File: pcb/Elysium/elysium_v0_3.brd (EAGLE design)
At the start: 64.8 x 105.1 mm, 20 parts, among them U1 TLC5940-NT, U2 TLC5940-NT, U3 TLC5940-NT, U4 TLC5940-NT

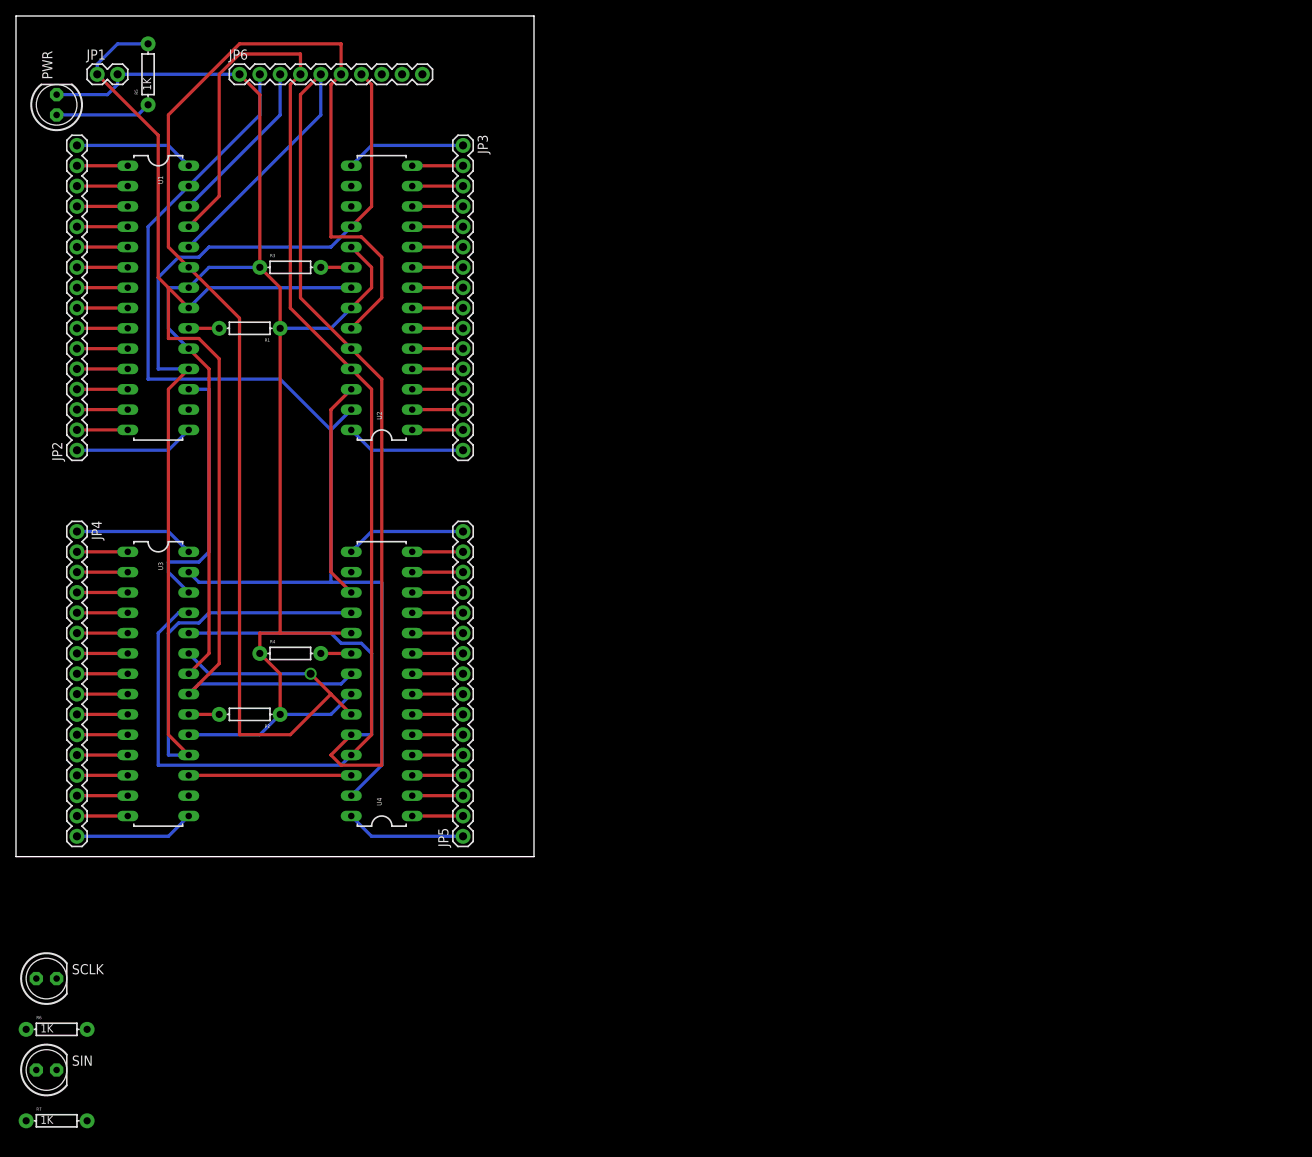
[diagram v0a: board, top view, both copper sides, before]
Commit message: Added rev_0_4 board
Rev 0_4 has status LEDs with ground planes.
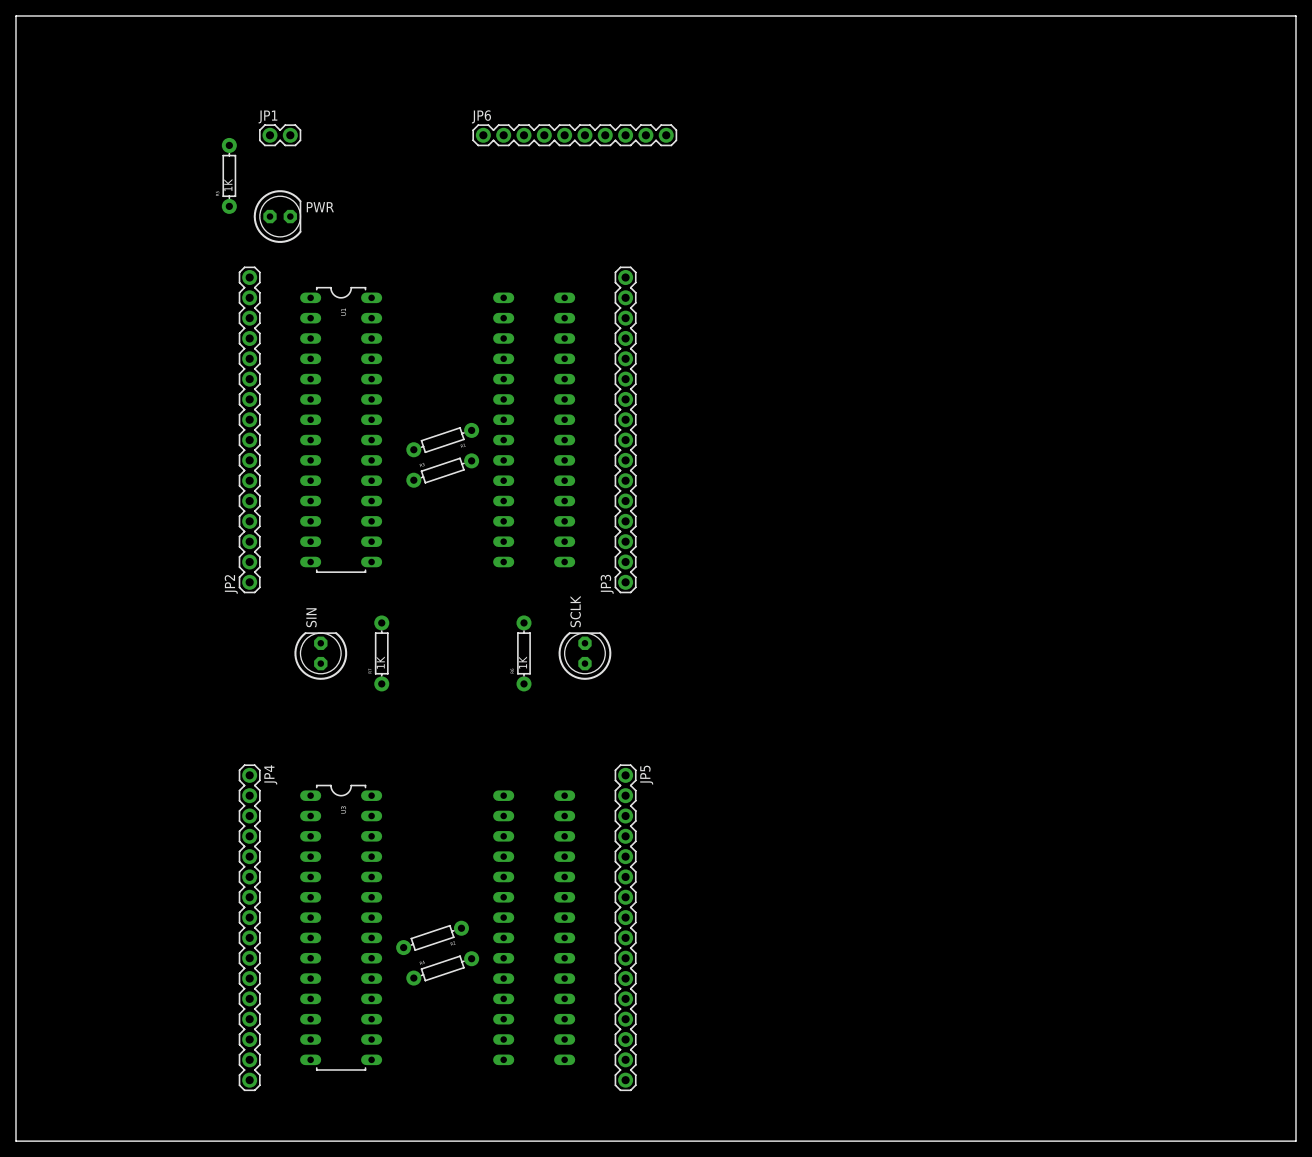
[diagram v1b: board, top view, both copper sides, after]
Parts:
- moved SCLK 78.6 mm to (71.1, 20.3), turned to 90 degrees
- moved R6 75.0 mm to (63.5, 20.3), turned to 90 degrees
- moved R7 71.2 mm to (45.7, 20.3), turned to 90 degrees
- moved SIN 62.3 mm to (38.1, 20.3), turned to 90 degrees
- moved JP3 58.3 mm to (76.2, 29.2), turned to 90 degrees
- moved R4 43.7 mm to (53.3, -19.1), turned to 18.5 degrees
- moved U3 38.1 mm to (40.6, -14.0)
- moved JP4 37.4 mm to (29.2, 5.08)
- moved R2 36.1 mm to (52.1, -15.2), turned to 198.5 degrees
- moved U4 35.9 mm to (64.8, -14.0), flipped to the bottom, turned to 270 degrees
- moved R3 31.8 mm to (53.3, 43.2), turned to 18.5 degrees
- moved JP6 31.4 mm to (58.4, 85.1)
- moved PWR 31.2 mm to (33.0, 74.9), turned to 0 degrees
- moved U1 28.2 mm to (40.6, 48.3)
- moved R1 27.9 mm to (53.3, 47.0), turned to 198.5 degrees
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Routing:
- net GND: track 225.2 -> 0.00 mm
- net BLANK: track 186.0 -> 0.00 mm, vias 1 -> 0
- net SCLK: track 171.3 -> 0.00 mm
- net XLAT: track 167.1 -> 0.00 mm
- net GSCLK: track 154.7 -> 0.00 mm
- net VPRG: track 144.9 -> 0.00 mm
- net VCC: track 142.6 -> 0.00 mm
- net N$65: track 33.3 -> 0.00 mm
- net N$67: track 27.5 -> 0.00 mm
- net SIN: track 21.2 -> 0.00 mm
- net N$66: track 20.3 -> 0.00 mm
- net N$64: track 15.0 -> 0.00 mm
- net N$49: track 15.0 -> 0.00 mm
- net N$33: track 15.0 -> 0.00 mm
- net N$32: track 15.0 -> 0.00 mm
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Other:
- board size 64.8 x 105.1 mm -> 160 x 140.6 mm
